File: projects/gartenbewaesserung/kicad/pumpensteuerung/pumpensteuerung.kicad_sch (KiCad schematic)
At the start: 7 parts, among them J2 Screw_Terminal_01x02, J3 I2C Terminal

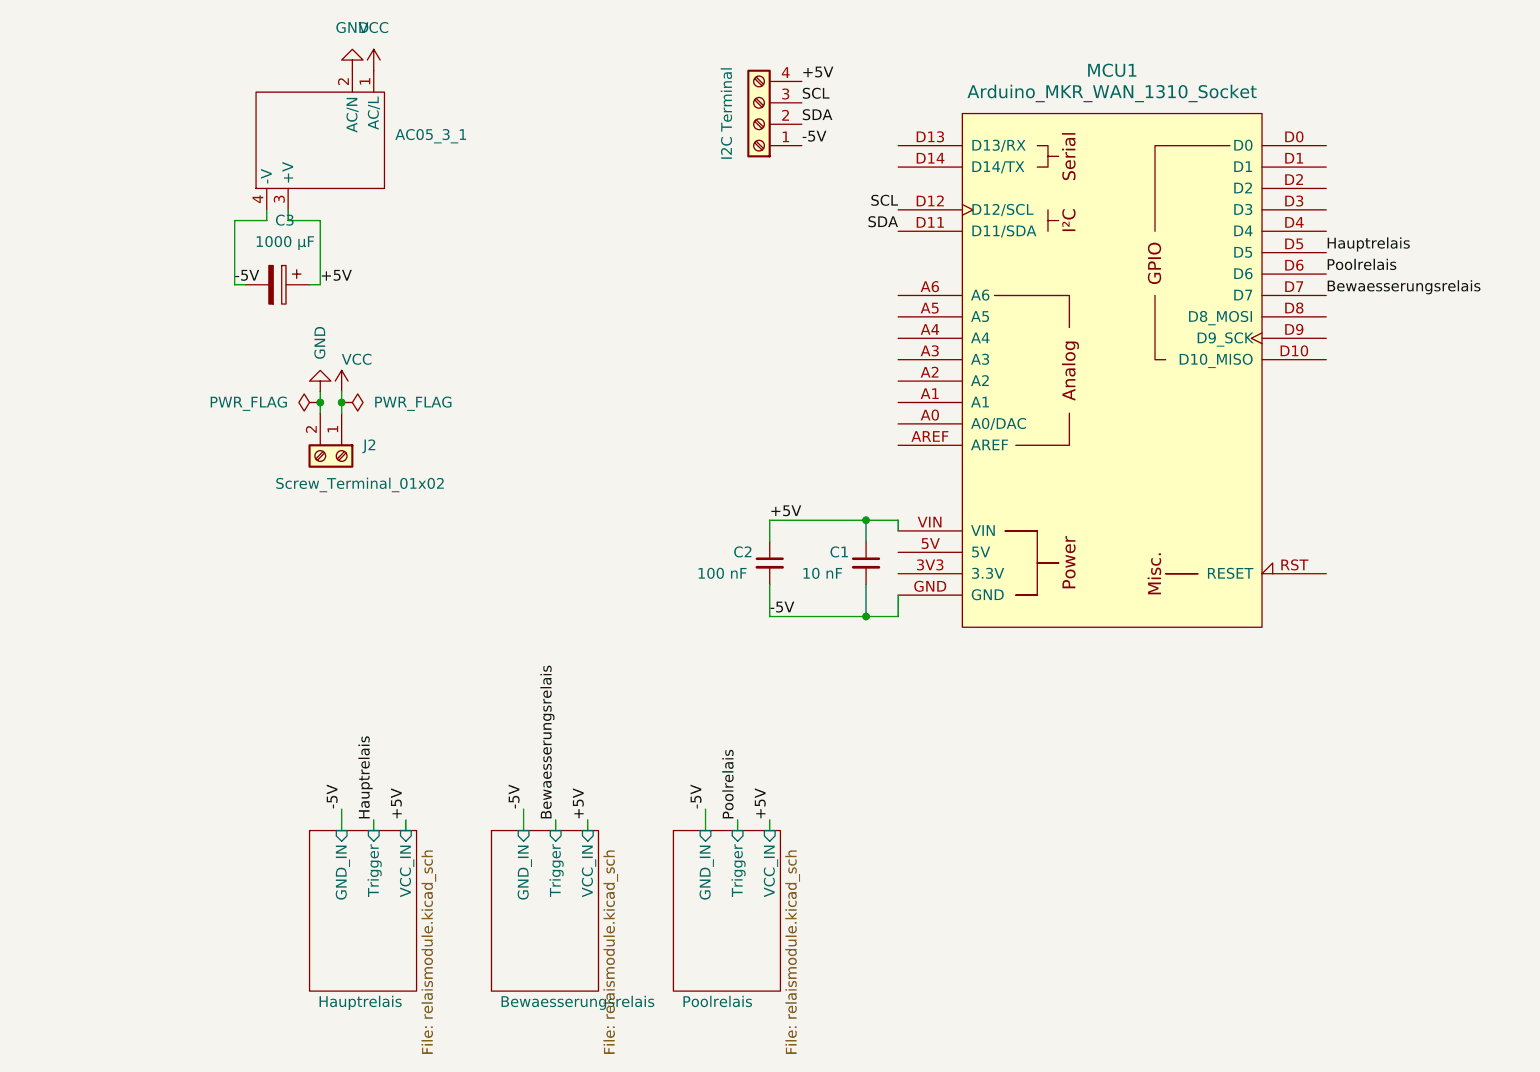
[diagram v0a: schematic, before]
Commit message: [gartenbewaesserung(pcb)] add MPN to easier pcb ordering
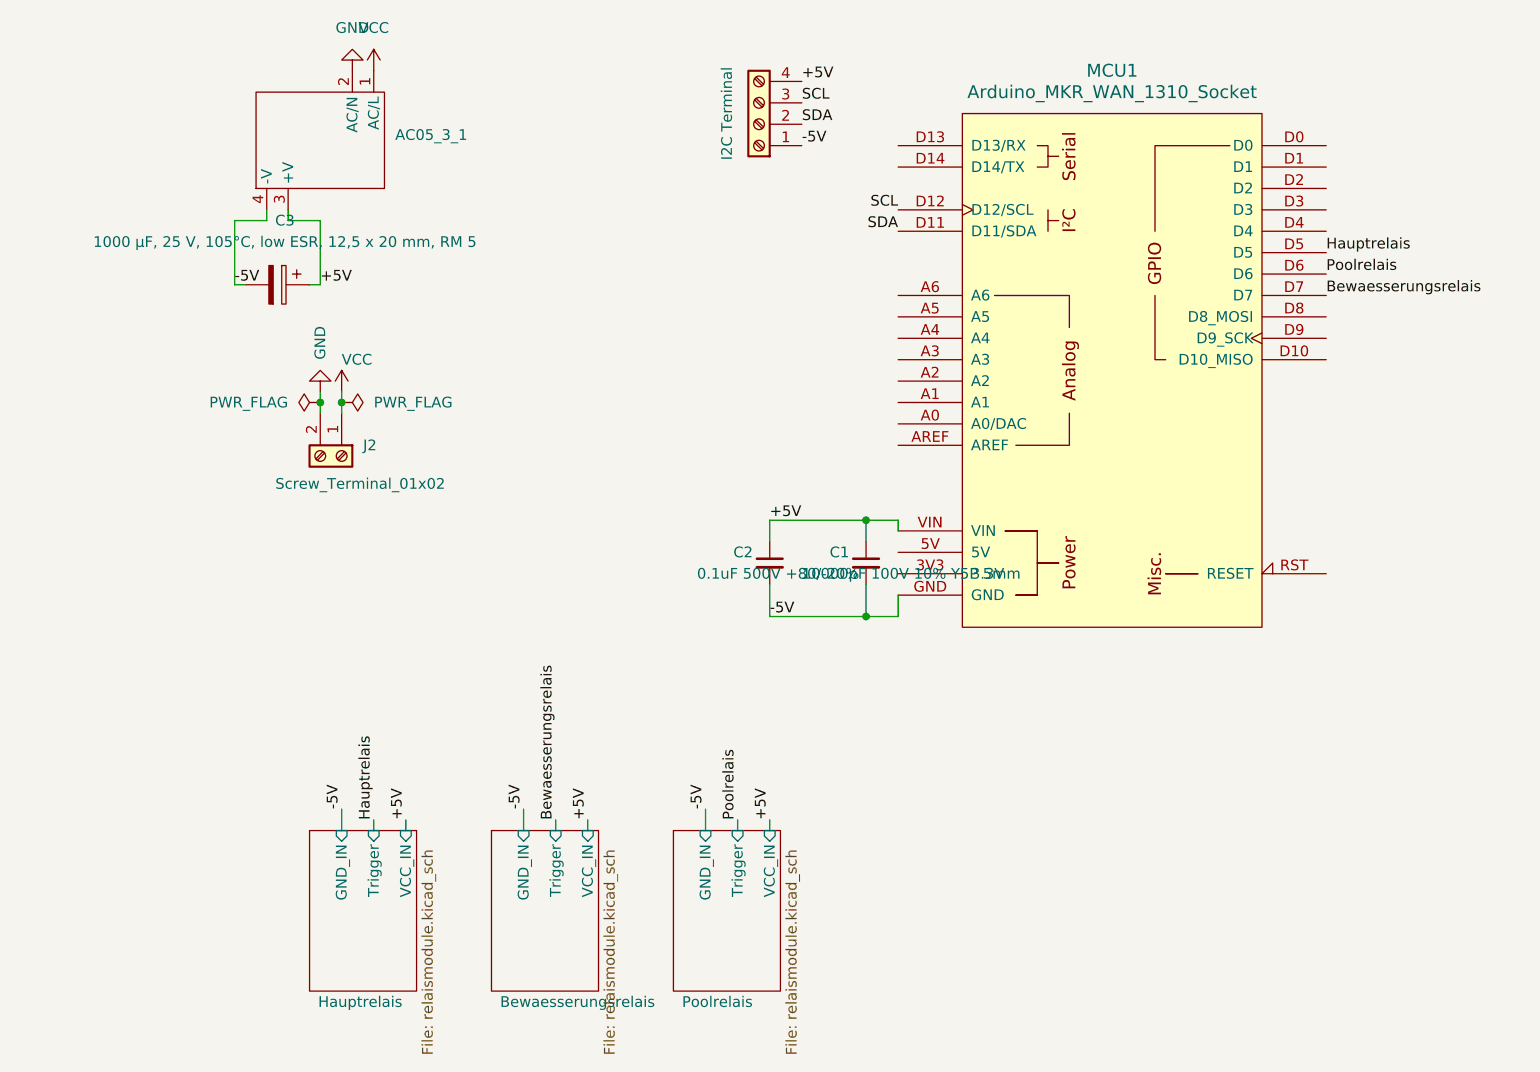
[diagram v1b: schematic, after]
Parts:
- C1: value 10 nF -> 10000pF 100V 10% Y5P 5mm; MPN (none) -> D103K43Y5PH6TJ5R
- C2: value 100 nF -> 0.1uF 500V +80/-20%; MPN (none) -> S104Z93Z5VL83L0R
- C3: value 1000 µF -> 1000 µF, 25 V, 105°C, low ESR, 12,5 x 20 mm, RM 5; MPN (none) -> EEUFM1E102
- J2: MPN (none) -> 1729128
- J3: MPN (none) -> 1729144
- MCU1: MPN (none) -> ABX00029
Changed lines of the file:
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@@
 			)
 		)
-		(property "Value" "10 nF"
+		(property "Value" "10000pF 100V 10% Y5P 5mm"
 			(at 83.82 77.47 0)
 			(effects
@@
 		)
 		(property "Description" "Unpolarized capacitor, small symbol"
+			(at 91.44 76.2 0)
+			(effects
+				(font
+					(size 1.27 1.27)
+				)
+				(hide yes)
+			)
+		)
+		(property "MPN" "D103K43Y5PH6TJ5R"
 			(at 91.44 76.2 0)
 			(effects
@@
 			)
 		)
+		(property "MPN" "ABX00029"
+			(at 120.65 53.34 0)
+			(effects
+				(font
+					(size 1.27 1.27)
+				)
+				(hide yes)
+			)
+		)
 		(pin "D4"
 		)
@@
 			)
 		)
-		(property "Value" "1000 µF"
+		(property "Value" "1000 µF, 25 V, 105°C, low ESR, 12,5 x 20 mm, RM 5"
 			(at 22.479 38.1 90)
 			(effects
@@
 			)
 		)
+		(property "MPN" "EEUFM1E102"
+			(at 21.59 43.18 90)
+			(effects
+				(font
+					(size 1.27 1.27)
+				)
+				(hide yes)
+			)
+		)
 		(pin "1"
 		)
@@
 			)
 		)
-		(property "Value" "100 nF"
+		(property "Value" "0.1uF 500V +80/-20%"
 			(at 71.374 77.47 0)
 			(effects
@@
 		)
 		(property "Description" "Unpolarized capacitor, small symbol"
+			(at 80.01 76.2 0)
+			(effects
+				(font
+					(size 1.27 1.27)
+				)
+				(hide yes)
+			)
+		)
+		(property "MPN" "S104Z93Z5VL83L0R"
 			(at 80.01 76.2 0)
 			(effects
@@
 			)
 		)
+		(property "MPN" "1729144"
+			(at 78.74 24.13 90)
+			(effects
+				(font
+					(size 1.27 1.27)
+				)
+				(hide yes)
+			)
+		)
 		(pin "1"
 		)
@@
 			(effects
 				(font
+					(size 1.27 1.27)
+				)
+				(hide yes)
+			)
+		)
+		(property "MPN" "1729128"
+			(at 29.21 63.5 90)
+			(effects
+				(font

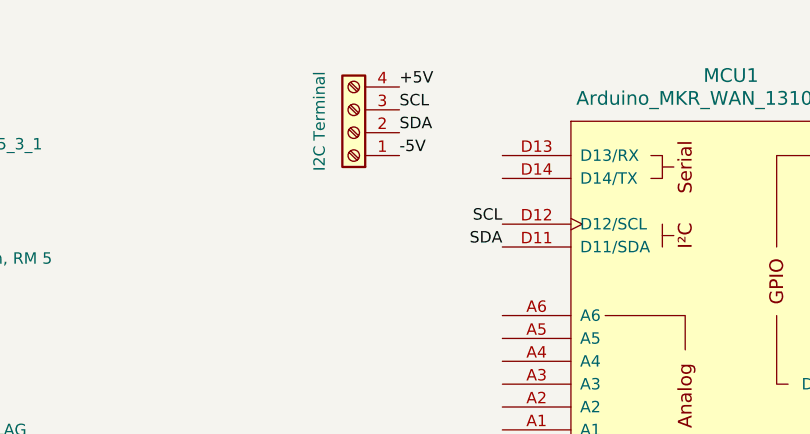
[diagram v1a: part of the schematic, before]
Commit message: [gartenbewaesserung(pcb)] remove screw terminal for i2c
currently we do not need it. and we will never do, we will use modbus
(rs485) to switch relais.

the relais module will be created later. and if we know that is the way
to go we will add rs485 functionality also to the pump.
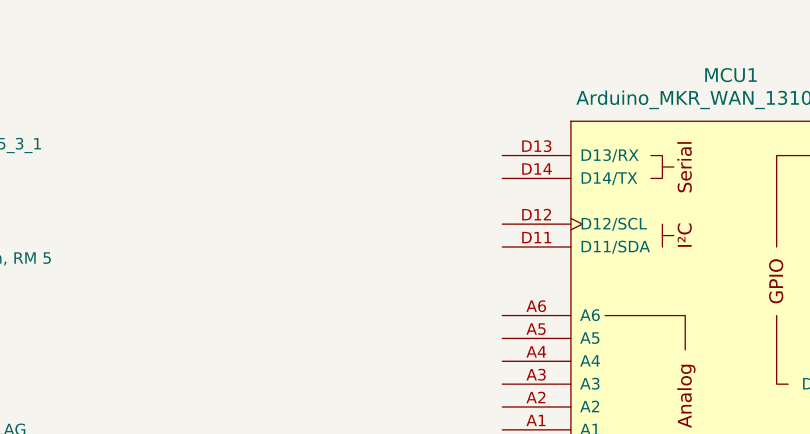
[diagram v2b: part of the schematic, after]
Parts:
- removed J3: I2C Terminal, PhoenixContact:MKDSN 1,5_4-5,08, symbol Connector:Screw_Terminal_01x04
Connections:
- net SCL: no longer names the net of MCU1.D12 (D12/SCL)
- net SDA: no longer names the net of MCU1.D11 (D11/SDA)
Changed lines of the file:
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@@
-		)
-	)
-	(label "-5V"
-		(at 83.82 26.67 0)
-		(effects
-			(font
-				(size 1.27 1.27)
-			)
-			(justify left bottom)
-		)
-	)
-	(label "SDA"
-		(at 95.25 36.83 180)
-		(effects
-			(font
-				(size 1.27 1.27)
-			)
-			(justify right bottom)
 		)
 	)
@@
 	)
 	(label "+5V"
-		(at 83.82 19.05 0)
-		(effects
-			(font
-				(size 1.27 1.27)
-			)
-			(justify left bottom)
-		)
-	)
-	(label "+5V"
 		(at 58.42 106.68 90)
 		(effects
@@
 		)
 	)
-	(label "SDA"
-		(at 83.82 24.13 0)
-		(effects
-			(font
-				(size 1.27 1.27)
-			)
-			(justify left bottom)
-		)
-	)
 	(label "-5V"
 		(at 72.39 105.41 90)
@@
 	(label "+5V"
 		(at 36.83 106.68 90)
-		(effects
-			(font
-				(size 1.27 1.27)
-			)
-			(justify left bottom)
-		)
-	)
-	(label "SCL"
-		(at 95.25 34.29 180)
-		(effects
-			(font
-				(size 1.27 1.27)
-			)
-			(justify right bottom)
-		)
-	)
-	(label "SCL"
-		(at 83.82 21.59 0)
 		(effects
 			(font
@@
 					(unit 1)
 				)
-			)
-		)
-	)
-	(symbol
-		(lib_id "Connector:Screw_Terminal_01x04")
-		(at 78.74 24.13 180)
-		(unit 1)
-		(exclude_from_sim no)
-		(in_bom yes)
-		(on_board yes)
-		(dnp no)
-		(fields_autoplaced yes)
-		(property "Reference" "J3"
-			(at 72.39 22.86 90)
-			(effects
-				(font
-					(size 1.27 1.27)
-				)
-				(hide yes)
-			)
-		)
-		(property "Value" "I2C Terminal"
-			(at 74.93 22.86 90)
-			(effects
-				(font
-					(size 1.27 1.27)
-				)
-			)
-		)
-		(property "Footprint" "PhoenixContact:MKDSN 1,5_4-5,08"
-			(at 78.74 24.13 0)
-			(effects
-				(font
-					(size 1.27 1.27)
-				)
-				(hide yes)
-			)
-		)
-		(property "Datasheet" "~"
-			(at 78.74 24.13 0)
-			(effects
-				(font
-					(size 1.27 1.27)
-				)
-				(hide yes)
-			)
-		)
-		(property "Description" "Generic screw terminal, single row, 01x04, script generated (kicad-library-utils/schlib/autogen/connector/)"
-			(at 78.74 24.13 0)
-			(effects
-				(font
-					(size 1.27 1.27)
-				)
-				(hide yes)
-			)
-		)
-		(property "MPN" "1729144"
-			(at 78.74 24.13 90)
-			(effects
-				(font
-					(size 1.27 1.27)
-				)
-				(hide yes)
-			)
-		)
-		(pin "1"
-		)
-		(pin "2"
-		)
-		(pin "3"
-		)
-		(pin "4"
-		)
-		(instances
-			(project ""
-				(path "/21a07dfa-371b-4773-840e-44a8dfeac208"
-					(reference "J3")
-					(unit 1)
-				)
